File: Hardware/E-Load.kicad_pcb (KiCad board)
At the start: 2 copper layers, 76.2 x 71.1 mm, 57 parts, among them J1 PJ-002A, J2 Conn_01x05_Male, J3 Conn_01x08_Male, J4 Screw_Terminal_01x02, Q1 PSMN5R2-60YL, SW2 SW_Push, SW3 SW_Push, SW4 SW_Push, U1 AP2210K-3.3, U2 STM32F103C8Tx, U3 DAC121C081CIMK, U4 TLV9102IPWR

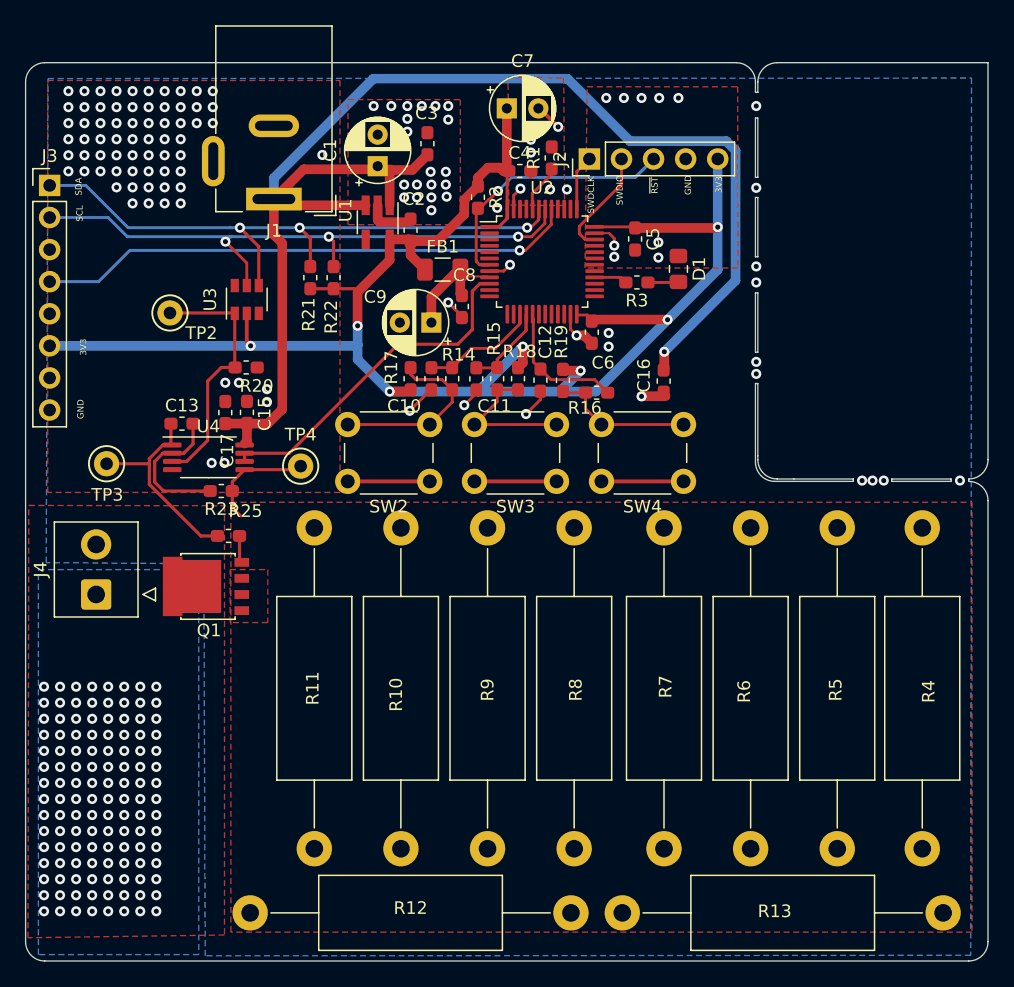
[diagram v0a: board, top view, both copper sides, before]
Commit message: Added a Quad opamp. fixed cut out, fixed silkscreen issues. Made pin names bigger
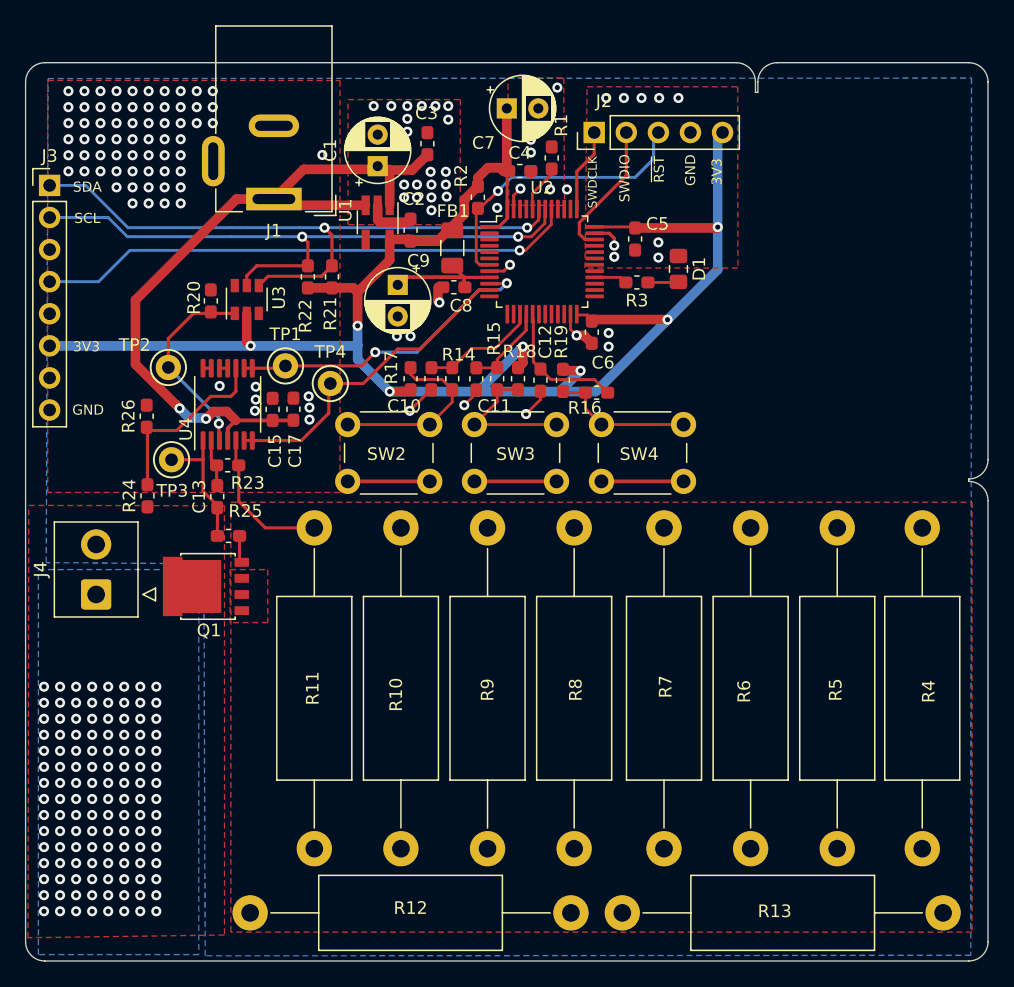
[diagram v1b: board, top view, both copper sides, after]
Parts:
- removed C16: 1n, Capacitor_SMD:C_0603_1608Metric_Pad1.05x0.95mm_HandSolder
- added R24: 5.6k, Resistor_SMD:R_0603_1608Metric_Pad1.05x0.95mm_HandSolder, F.Cu at (104.7, 99.0)
- added R26: 50k, Resistor_SMD:R_0603_1608Metric_Pad1.05x0.95mm_HandSolder, F.Cu at (104.6, 92.7)
- added TP1: TestPoint_Alt, TestPoint:TestPoint_Keystone_5000-5004_Miniature, F.Cu at (115.6, 88.7)
- U4: value TLV9102IPWR -> MCP6H04; footprint Package_SO:TSSOP-8_4.4x3mm_P0.65mm -> Package_SO:TSSOP-14_4.4x5mm_P0.65mm
- moved TP4 6.95 mm to (119.2, 90.1)
- moved C13 6.42 mm to (110.2, 99.1), turned to 90 degrees
- moved R20 5.97 mm to (109.7, 83.6), turned to 270 degrees
- moved C17 5.40 mm to (116.3, 92.1)
- moved TP3 5.15 mm to (106.6, 96.1)
- moved U4 4.46 mm to (111.1, 91.8), turned to 90 degrees
- moved TP2 4.32 mm to (106.4, 88.8)
- moved C9 4.00 mm to (124.5, 82.3), turned to 270 degrees
- moved J2 2.13 mm to (140.1, 70.2)
- moved R23 2.09 mm to (111.1, 96.6)
- moved C15 2.05 mm to (114.6, 92.2)
- moved R22 2.03 mm to (117.4, 81.7)
- moved FB1 1.88 mm to (128.8, 79.4), turned to 270 degrees
- moved R21 1.72 mm to (119.3, 81.7)
- moved C8 1.65 mm to (129.0, 82.5), turned to 180 degrees
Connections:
- TP4 pad 1: /CurrentControl/Vmeas -> /CurrentControl/Current_ADC
- U2 pad 10: /CurrentControl/ADC -> /CurrentControl/Vin_ADC
- U2 pad 11: (no net) -> /CurrentControl/Current_ADC
- U4 pad 4: GND -> +12V
- U4 pad 6: /CurrentControl/ADC -> /CurrentControl/Current_ADC
- U4 pad 7: /CurrentControl/ADC -> /CurrentControl/Current_ADC
- U4 pad 8: +12V -> /CurrentControl/Vin_ADC
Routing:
- net +12V: track 111.9 -> 60.9 mm, vias 1 -> 2
- net /CurrentControl/ADC: track 27.4 -> 0.00 mm
- net /CurrentControl/Current_ADC: track 0.00 -> 26.5 mm
- net /CurrentControl/Vin_ADC: track 0.00 -> 25.0 mm, vias 0 -> 2
- net Net-(R24-Pad2): track 0.00 -> 14.9 mm
- net Net-(C13-Pad2): track 11.5 -> 3.76 mm
- net Net-(C13-Pad1): track 16.5 -> 10.5 mm
- net Net-(R20-Pad2): track 20.2 -> 15.8 mm, vias 0 -> 1
- net GND: track 46.0 -> 42.0 mm, vias 125 -> 117
- net /MCU/SWDCLK: track 4.38 -> 8.04 mm
- net +3V3: track 143.0 -> 146.6 mm
- net /CurrentControl/Vmeas: track 8.89 -> 11.8 mm
- net /MCU/~RST: track 22.9 -> 25.2 mm
- net /MCU/SWDIO: track 10.2 -> 11.6 mm
- net /CurrentControl/SCL: track 48.7 -> 49.8 mm, vias 3 -> 2
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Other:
- outline, holes or cut-outs redrawn

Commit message: forgot to save
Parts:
- moved R26 11.3 mm to (114.8, 97.5), turned to 180 degrees
- moved R25 4.24 mm to (109.0, 98.5), turned to 90 degrees
- moved R23 2.25 mm to (112.3, 98.5), turned to 90 degrees
- moved TP3 1.85 mm to (105.4, 94.7)
- moved R24 1.22 mm to (105.8, 99.6), turned to 270 degrees
- moved C13 0.72 mm to (110.7, 98.5)
- moved TP1 0.09 mm to (115.6, 88.8)
- moved U4 0.09 mm to (111.0, 91.8)
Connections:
- R24 pad 1: VCC -> Net-(R24-Pad1)
- R24 pad 2: Net-(R24-Pad2) -> VCC
- R26 pad 1: Net-(R24-Pad2) -> GND
- R26 pad 2: GND -> Net-(R24-Pad1)
- U4 pad 10: Net-(R24-Pad2) -> /CurrentControl/Vmeas
- U4 pad 5: /CurrentControl/Vmeas -> Net-(R24-Pad1)
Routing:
- net Net-(R24-Pad2): track 14.9 -> 0.00 mm
- net Net-(R24-Pad1): track 0.00 -> 12.4 mm, vias 0 -> 2
- net /CurrentControl/Vmeas: track 11.8 -> 17.4 mm, vias 0 -> 1
- net Net-(Q1-Pad4): track 2.16 -> 6.20 mm
- net Net-(C13-Pad1): track 10.5 -> 9.18 mm
- net Net-(C13-Pad2): track 3.76 -> 4.92 mm
- net GND: vias 117 -> 121
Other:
- outline, holes or cut-outs redrawn

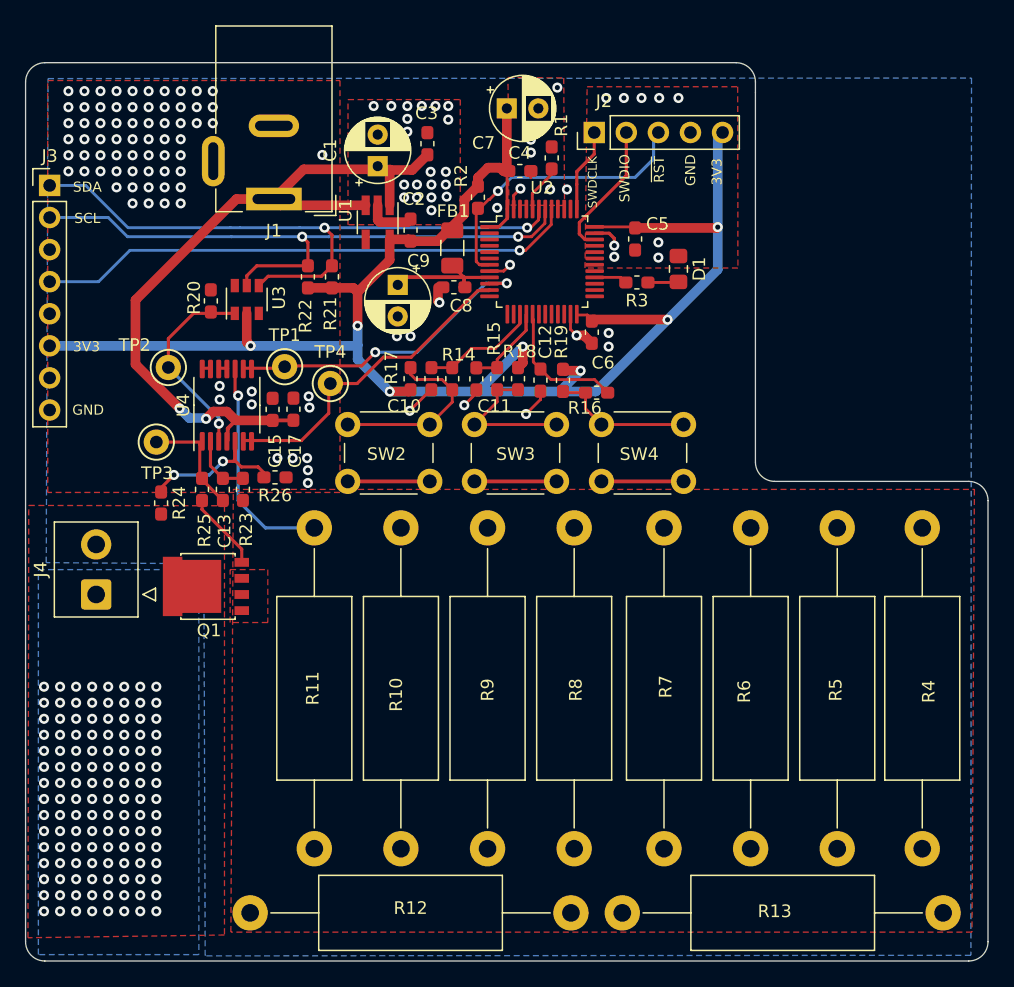
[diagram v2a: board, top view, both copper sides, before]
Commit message: Added LCSC part#, Thermal vias, etc
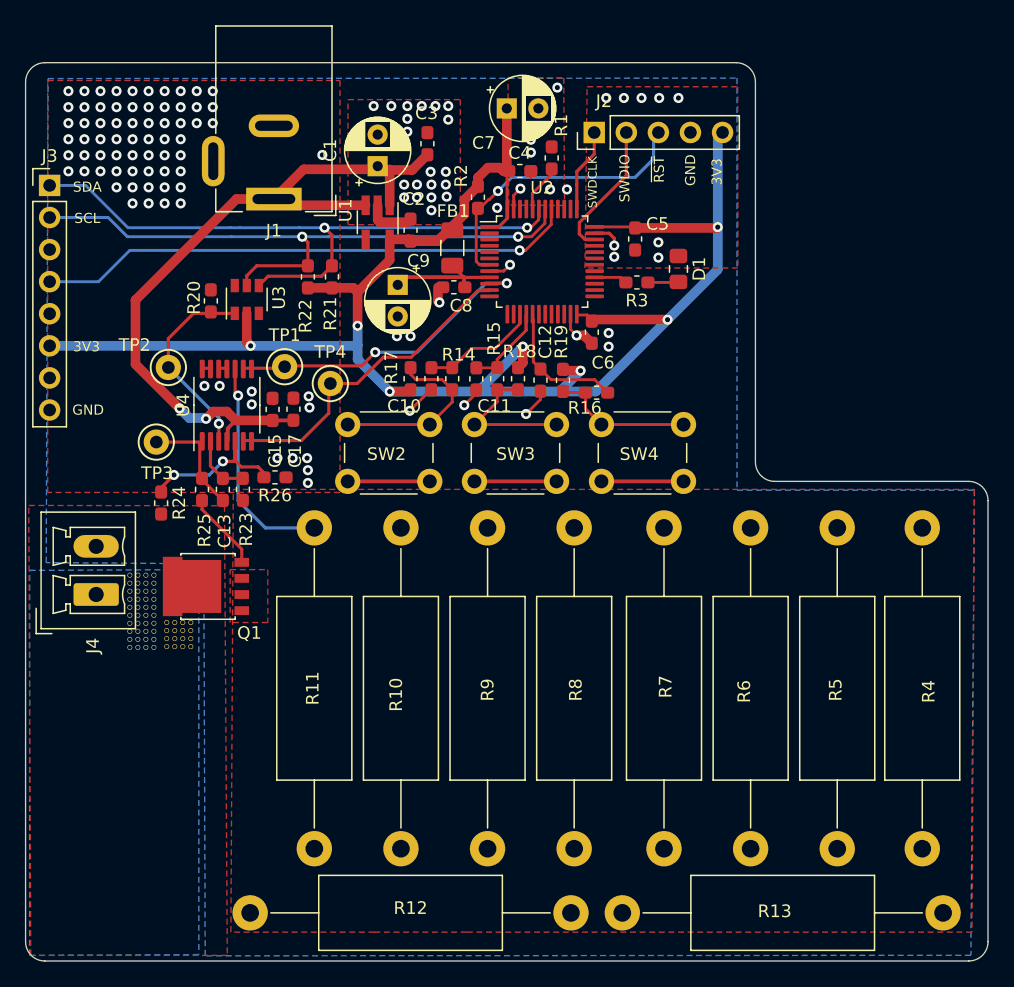
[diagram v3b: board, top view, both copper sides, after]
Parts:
- added REF**: ThermalVia, ThermalVias:ThermalVia, F.Cu at (103.3, 108.5)
- added REF**: ThermalVia, ThermalVias:ThermalVia, F.Cu at (105.2, 109.7)
- added REF**: ThermalVia, ThermalVias:ThermalVia, F.Cu at (104.6, 109.7)
- added REF**: ThermalVia, ThermalVias:ThermalVia, F.Cu at (103.9, 109.7)
- added REF**: ThermalVia, ThermalVias:ThermalVia, F.Cu at (103.3, 109.7)
- added REF**: ThermalVia, ThermalVias:ThermalVia, F.Cu at (105.2, 109.1)
- added REF**: ThermalVia, ThermalVias:ThermalVia, F.Cu at (104.6, 109.1)
- added REF**: ThermalVia, ThermalVias:ThermalVia, F.Cu at (103.9, 109.1)
- added REF**: ThermalVia, ThermalVias:ThermalVia, F.Cu at (103.3, 109.1)
- added REF**: ThermalVia, ThermalVias:ThermalVia, F.Cu at (105.2, 108.5)
- added REF**: ThermalVia, ThermalVias:ThermalVia, F.Cu at (104.6, 108.5)
- added REF**: ThermalVia, ThermalVias:ThermalVia, F.Cu at (105.2, 111.0)
- added REF**: ThermalVia, ThermalVias:ThermalVia, F.Cu at (103.9, 108.5)
- added REF**: ThermalVia, ThermalVias:ThermalVia, F.Cu at (105.2, 107.8)
- added REF**: ThermalVia, ThermalVias:ThermalVia, F.Cu at (104.6, 107.8)
- added REF**: ThermalVia, ThermalVias:ThermalVia, F.Cu at (103.9, 107.8)
- added REF**: ThermalVia, ThermalVias:ThermalVia, F.Cu at (103.3, 107.8)
- added REF**: ThermalVia, ThermalVias:ThermalVia, F.Cu at (105.2, 107.2)
- added REF**: ThermalVia, ThermalVias:ThermalVia, F.Cu at (104.6, 107.2)
- added REF**: ThermalVia, ThermalVias:ThermalVia, F.Cu at (103.9, 107.2)
- added REF**: ThermalVia, ThermalVias:ThermalVia, F.Cu at (103.3, 107.2)
- added REF**: ThermalVia, ThermalVias:ThermalVia, F.Cu at (105.2, 106.6)
- added REF**: ThermalVia, ThermalVias:ThermalVia, F.Cu at (104.6, 111.0)
- added REF**: ThermalVia, ThermalVias:ThermalVia, F.Cu at (104.6, 106.6)
- added REF**: ThermalVia, ThermalVias:ThermalVia, F.Cu at (103.9, 106.6)
- added REF**: ThermalVia, ThermalVias:ThermalVia, F.Cu at (103.3, 106.6)
- added REF**: ThermalVia, ThermalVias:ThermalVia, F.Cu at (105.2, 105.9)
- added REF**: ThermalVia, ThermalVias:ThermalVia, F.Cu at (104.6, 105.9)
- added REF**: ThermalVia, ThermalVias:ThermalVia, F.Cu at (103.9, 105.9)
- added REF**: ThermalVia, ThermalVias:ThermalVia, F.Cu at (103.3, 105.9)
- added REF**: ThermalVia, ThermalVias:ThermalVia, F.Cu at (105.2, 105.3)
- added REF**: ThermalVia, ThermalVias:ThermalVia, F.Cu at (104.6, 105.3)
- added REF**: ThermalVia, ThermalVias:ThermalVia, F.Cu at (103.9, 105.3)
- added REF**: ThermalVia, ThermalVias:ThermalVia, F.Cu at (103.9, 111.0)
- added REF**: ThermalVia, ThermalVias:ThermalVia, F.Cu at (103.3, 105.3)
- added REF**: ThermalVia, ThermalVias:ThermalVia, F.Cu at (108.1, 110.9)
- added REF**: ThermalVia, ThermalVias:ThermalVia, F.Cu at (107.5, 110.9)
- added REF**: ThermalVia, ThermalVias:ThermalVia, F.Cu at (106.9, 110.9)
- added REF**: ThermalVia, ThermalVias:ThermalVia, F.Cu at (106.2, 110.9)
- added REF**: ThermalVia, ThermalVias:ThermalVia, F.Cu at (108.1, 110.3)
- added REF**: ThermalVia, ThermalVias:ThermalVia, F.Cu at (107.5, 110.3)
- added REF**: ThermalVia, ThermalVias:ThermalVia, F.Cu at (106.9, 110.3)
- added REF**: ThermalVia, ThermalVias:ThermalVia, F.Cu at (106.2, 110.3)
- added REF**: ThermalVia, ThermalVias:ThermalVia, F.Cu at (108.1, 109.7)
- added REF**: ThermalVia, ThermalVias:ThermalVia, F.Cu at (103.3, 111.0)
- added REF**: ThermalVia, ThermalVias:ThermalVia, F.Cu at (107.5, 109.7)
- added REF**: ThermalVia, ThermalVias:ThermalVia, F.Cu at (106.9, 109.7)
- added REF**: ThermalVia, ThermalVias:ThermalVia, F.Cu at (106.2, 109.7)
- added REF**: ThermalVia, ThermalVias:ThermalVia, F.Cu at (108.1, 109.0)
- added REF**: ThermalVia, ThermalVias:ThermalVia, F.Cu at (107.5, 109.0)
- added REF**: ThermalVia, ThermalVias:ThermalVia, F.Cu at (106.9, 109.0)
- added REF**: ThermalVia, ThermalVias:ThermalVia, F.Cu at (106.2, 109.0)
- added REF**: ThermalVia, ThermalVias:ThermalVia, F.Cu at (105.2, 110.4)
- added REF**: ThermalVia, ThermalVias:ThermalVia, F.Cu at (104.6, 110.4)
- added REF**: ThermalVia, ThermalVias:ThermalVia, F.Cu at (103.9, 110.4)
- added REF**: ThermalVia, ThermalVias:ThermalVia, F.Cu at (103.3, 110.4)
- C10: value 0.1uF -> 1u
- C3: value 0.1uF -> 100nF
- J4: footprint Connector_TE-Connectivity:TE_826576-2_1x02_P3.96mm_Vertical -> Connector_Phoenix_MC:PhoenixContact_MCV_1,5_2-G-3.81_1x02_P3.81mm_Vertical
- R25: value 50 -> 75
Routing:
- net VCC: vias 120 -> 0
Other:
- rule via_min_size: 0.4 -> 0.45
